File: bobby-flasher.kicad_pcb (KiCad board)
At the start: 2 copper layers, 17.4 x 29.4 mm, 30 parts, among them J1 Conn_01x03, J2 Conn_01x06, J3 Flash, Q1 SS8050_C2150, Q2 SS8050_C2150, U1 CH343G, U2 AMS1117-3.3

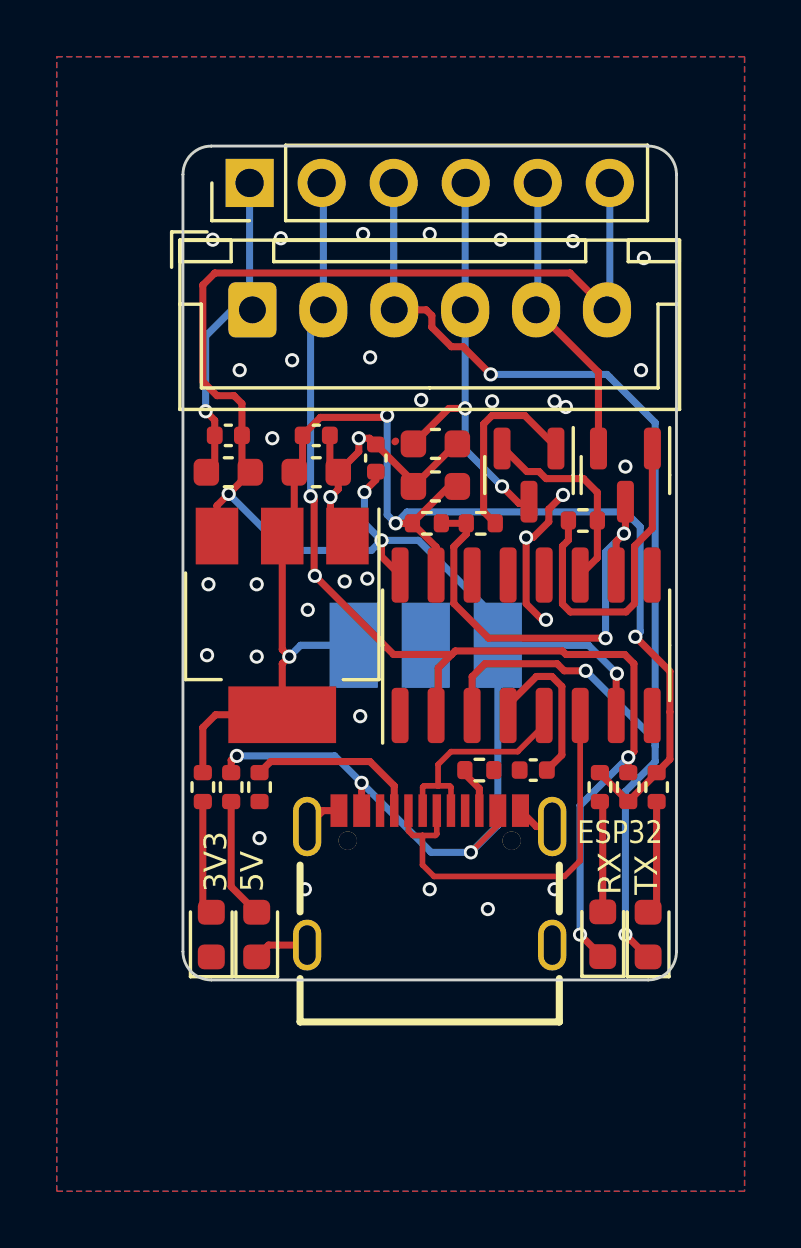
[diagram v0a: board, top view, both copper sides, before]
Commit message: Ordered at JLCPCB; remove unconnected resistor from schematic; mark NPTH holes of USB-C as NPTH; fix connection of transistor in PCB file; replace unavailable LEDs with alternatives
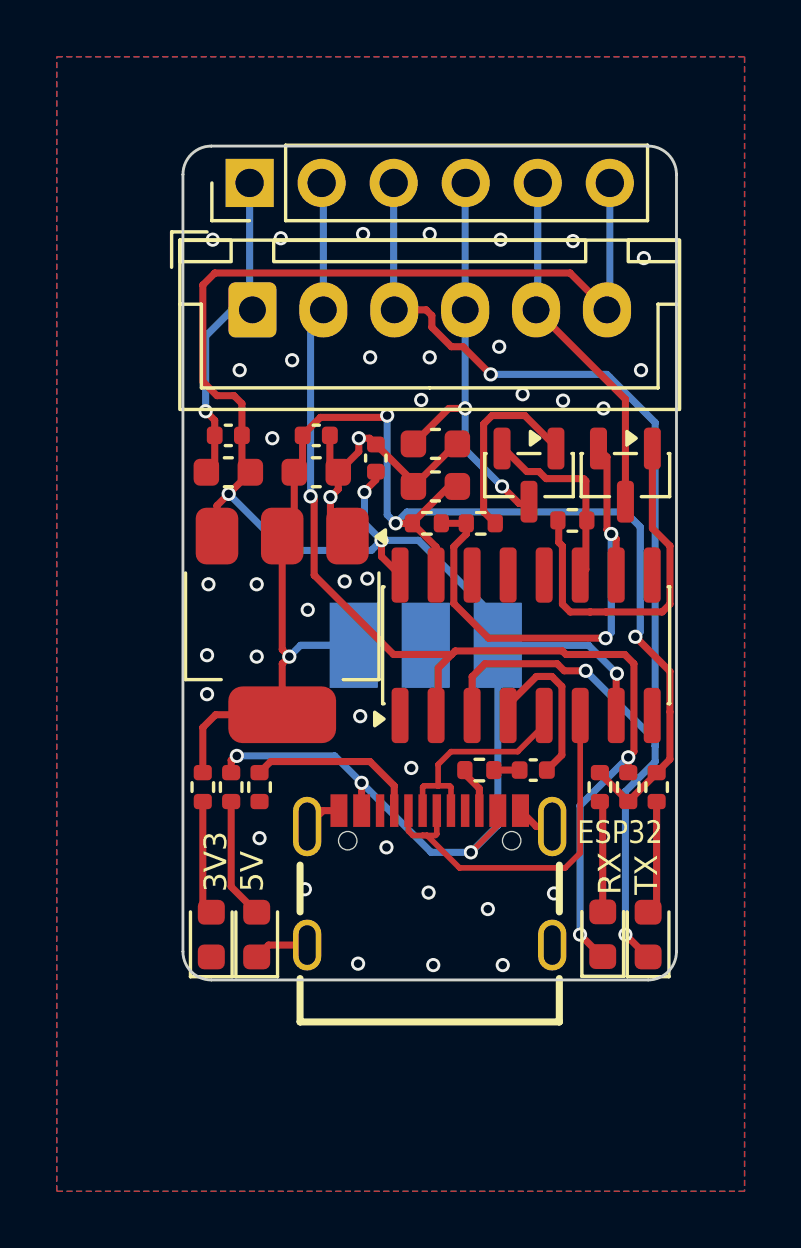
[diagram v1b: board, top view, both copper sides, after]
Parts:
- moved R5 0.37 mm to (5.03, 64.8)
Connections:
- Q2 pad 2: IO0 -> DTR
- Q2 pad 3: DTR -> IO0
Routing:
- net GND: track 32.1 -> 27.6 mm, vias 36 -> 40
- net IO0: track 10.2 -> 12.6 mm
- net DTR: track 16.4 -> 18.2 mm
- net Net-(Q2-B): track 11.6 -> 12.8 mm
- net USB_DN: track 14.7 -> 13.7 mm
- net ESP_RX: vias 4 -> 3
